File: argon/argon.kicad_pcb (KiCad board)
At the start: 2 copper layers, 60 x 60 mm, 77 parts, among them J1 USB, J2 V3V3-GND, J3 V3V3-GND, J4 V3V3-GND, J5 V3V3-GND, J6 V3V3-GND, J7 V3V3-GND, U1 LMC555xM, U2 AMS1117-3.3, U3 93LCxxA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

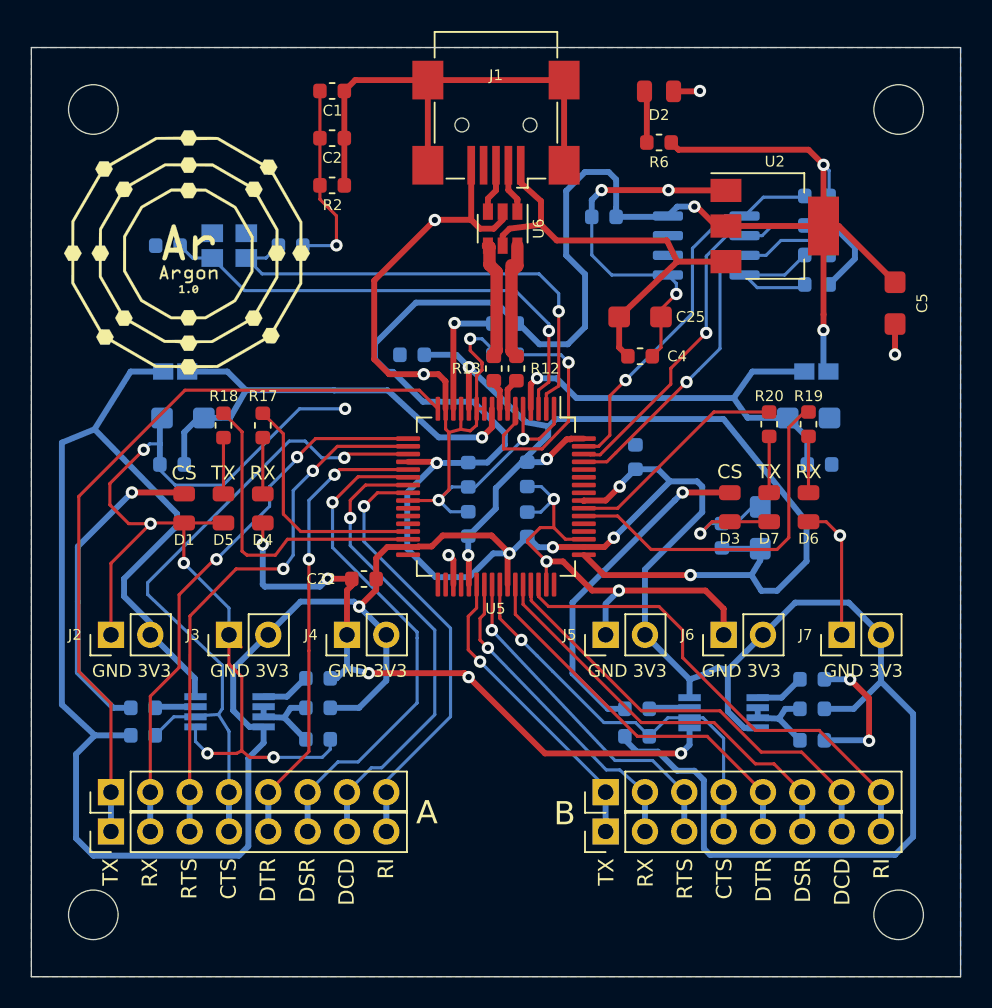
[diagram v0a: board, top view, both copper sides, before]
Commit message: GND on front & fix paths
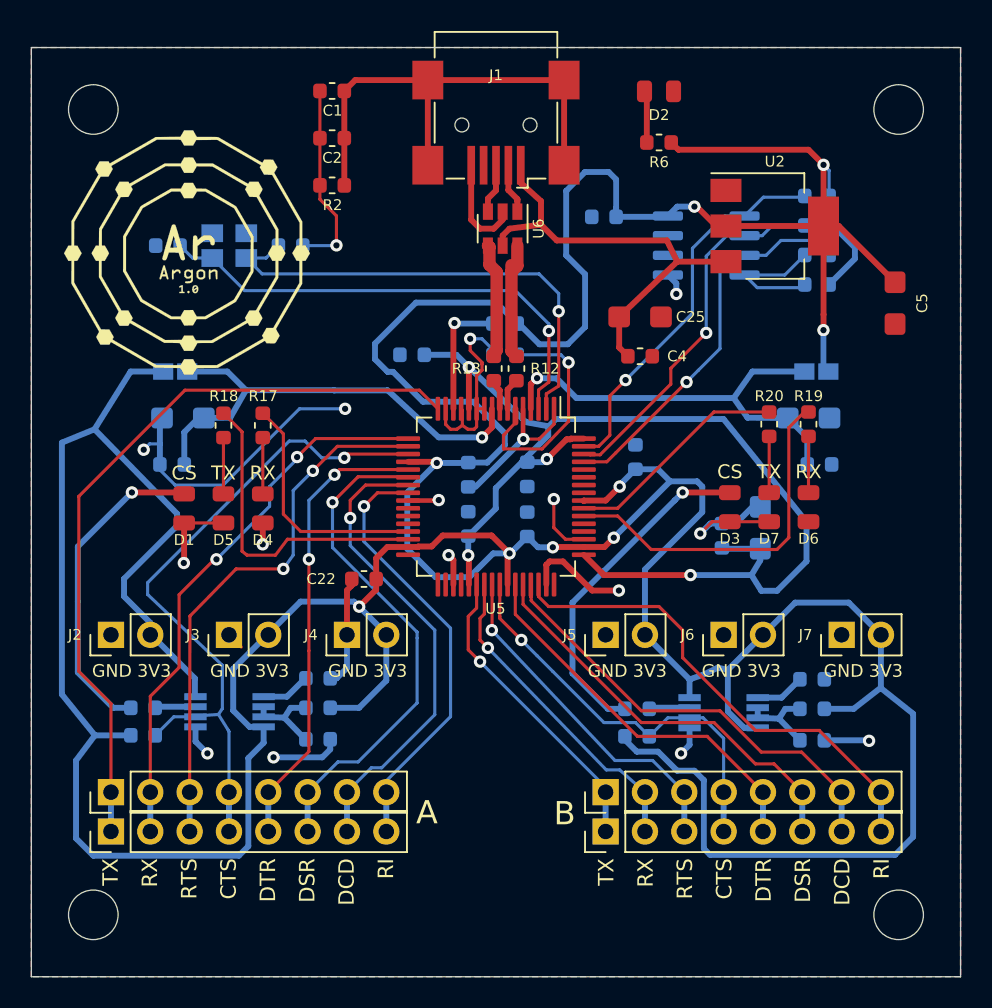
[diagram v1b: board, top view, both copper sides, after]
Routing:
- net GND: track 273.3 -> 114.4 mm, vias 30 -> 17
- net V3V3: track 343.0 -> 342.4 mm
- added copper zone on F.Cu, net GND

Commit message: Move capacitor & add filled zone near USB
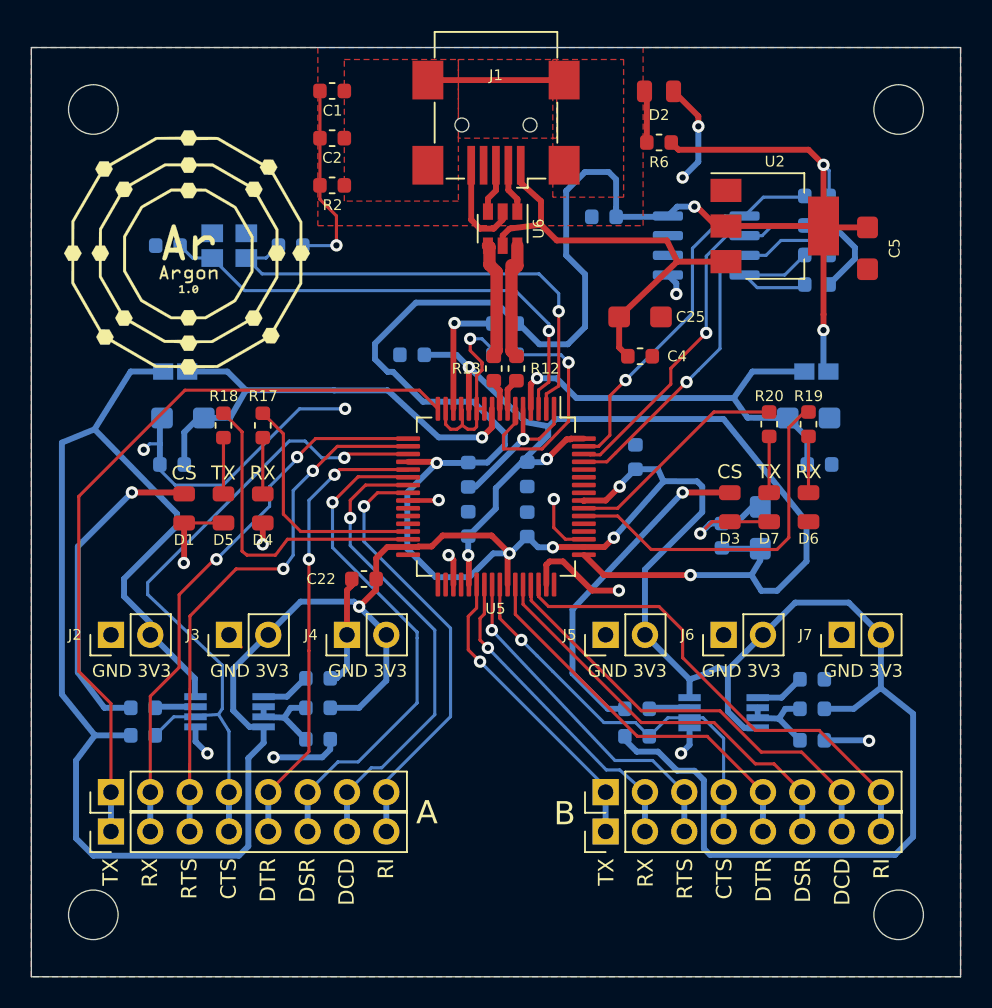
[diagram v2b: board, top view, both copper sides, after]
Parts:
- moved C5 3.96 mm to (174.0, 93.0)
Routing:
- net Net-(C1-Pad2): track 31.6 -> 8.80 mm
- net GND: track 114.4 -> 121.0 mm, vias 17 -> 19
- net V3V3: track 342.4 -> 339.1 mm
- added copper zone on F.Cu, net Net-(C1-Pad2)

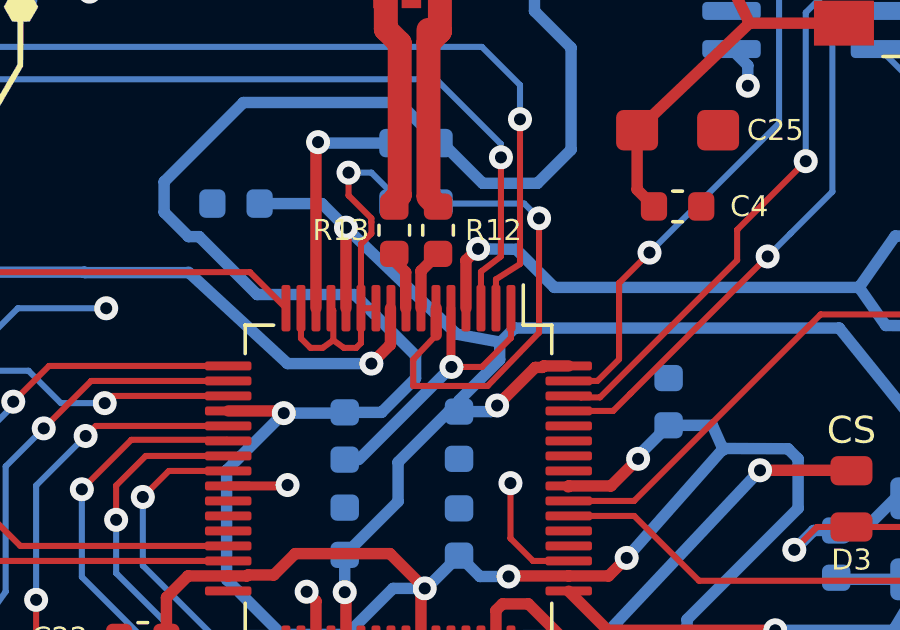
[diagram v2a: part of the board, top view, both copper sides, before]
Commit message: Fix connected pins on ftdi
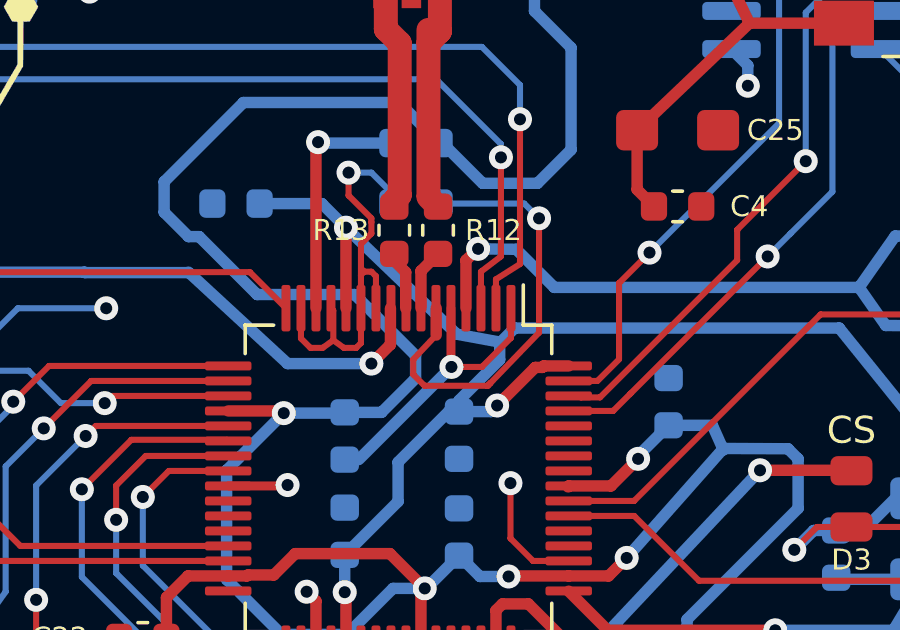
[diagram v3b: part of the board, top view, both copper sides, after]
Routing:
- net GND: track 121.0 -> 122.4 mm
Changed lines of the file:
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@@
     (thickness 1.6)
     (drawings 46)
-    (tracks 703)
+    (tracks 713)
     (zones 0)
     (modules 77)
@@
     (0 F.Cu signal)
     (31 B.Cu signal)
-    (32 B.Adhes user)
-    (33 F.Adhes user)
+    (32 B.Adhes user hide)
+    (33 F.Adhes user hide)
     (34 B.Paste user)
     (35 F.Paste user hide)
-    (36 B.SilkS user)
+    (36 B.SilkS user hide)
     (37 F.SilkS user)
-    (38 B.Mask user)
+    (38 B.Mask user hide)
     (39 F.Mask user hide)
     (40 Dwgs.User user)
-    (41 Cmts.User user)
+    (41 Cmts.User user hide)
     (42 Eco1.User user hide)
-    (43 Eco2.User user)
+    (43 Eco2.User user hide)
     (44 Edge.Cuts user)
     (45 Margin user hide)
@@
   )
   (setup
-    (last_trace_width 0.381)
+    (last_trace_width 0.2032)
     (user_trace_width 0.2032)
     (user_trace_width 0.3)
@@
   (segment (start 139.3 120.7295) (end 139.7105 120.7295) (width 0.381) (layer B.Cu) (net 1))
   (segment (start 130.5975 123.8635) (end 130.9755 123.8635) (width 0.381) (layer B.Cu) (net 1))
-  (segment (start 148.75 103.325) (end 148.75 101.186) (width 0.2032) (layer F.Cu) (net 1))
   (segment (start 148.75 101.186) (end 149.098 100.838) (width 0.2032) (layer F.Cu) (net 1))
   (segment (start 149.098 100.838) (end 149.098 100.457) (width 0.2032) (layer F.Cu) (net 1))
@@
   (segment (start 149.098 100.33) (end 148.336 99.568) (width 0.2032) (layer F.Cu) (net 1))
   (segment (start 148.336 99.568) (end 148.336 98.806) (width 0.2032) (layer F.Cu) (net 1))
-  (segment (start 149.25 103.325) (end 148.75 103.325) (width 0.2032) (layer F.Cu) (net 1))
   (segment (start 167.64 110.6175) (end 165.1 110.6175) (width 0.2032) (layer F.Cu) (net 1))
   (segment (start 165.1 110.6175) (end 163.9565 110.6175) (width 0.2032) (layer F.Cu) (net 1))
@@
   (via (at 162.052 88.392) (size 0.8) (drill 0.4) (layers F.Cu B.Cu) (net 1))
   (segment (start 163.068 87.376) (end 162.052 88.392) (width 0.381) (layer B.Cu) (net 1))
+  (segment (start 149.25 103.325) (end 149.25 102.26) (width 0.2032) (layer F.Cu) (net 1))
+  (segment (start 149.25 102.26) (end 149.098 102.108) (width 0.2032) (layer F.Cu) (net 1))
+  (segment (start 148.858 102.108) (end 148.75 102) (width 0.2032) (layer F.Cu) (net 1))
+  (segment (start 149.098 102.108) (end 148.858 102.108) (width 0.2032) (layer F.Cu) (net 1))
+  (segment (start 148.75 102) (end 148.75 101.186) (width 0.2032) (layer F.Cu) (net 1))
+  (segment (start 148.75 102.216) (end 148.858 102.108) (width 0.2032) (layer F.Cu) (net 1))
+  (segment (start 148.75 102.25) (end 148.75 102) (width 0.2032) (layer F.Cu) (net 1))
+  (segment (start 148.75 102.25) (end 148.75 102.216) (width 0.2032) (layer F.Cu) (net 1))
+  (segment (start 148.75 103.325) (end 148.75 102.25) (width 0.2032) (layer F.Cu) (net 1))
   (segment (start 136.503 121.9135) (end 137.687 120.7295) (width 0.381) (layer B.Cu) (net 2))
   (segment (start 134.9595 121.9135) (end 136.503 121.9135) (width 0.381) (layer B.Cu) (net 2))
@@
   (segment (start 154.686 100.33) (end 154.194 99.838) (width 0.2032) (layer B.Cu) (net 9))
   (segment (start 154.686 104.14) (end 154.686 100.33) (width 0.2032) (layer F.Cu) (net 9))
-  (segment (start 152.9715 105.918) (end 154.686 104.14) (width 0.2032) (layer F.Cu) (net 9))
-  (segment (start 150.495 105.918) (end 152.9715 105.918) (width 0.2032) (layer F.Cu) (net 9))
   (segment (start 151.25801 104.22051) (end 150.495 105.029) (width 0.2032) (layer F.Cu) (net 9))
-  (segment (start 150.495 105.029) (end 150.495 105.918) (width 0.2032) (layer F.Cu) (net 9))
+  (segment (start 150.495 105.029) (end 150.495 105.537) (width 0.2032) (layer F.Cu) (net 9))
+  (segment (start 152.974437 105.911601) (end 153.065019 105.821019) (width 0.2032) (layer F.Cu) (net 9))
+  (segment (start 150.869601 105.911601) (end 152.974437 105.911601) (width 0.2032) (layer F.Cu) (net 9))
+  (segment (start 150.495 105.537) (end 150.869601 105.911601) (width 0.2032) (layer F.Cu) (net 9))
+  (segment (start 152.9715 105.918) (end 153.065019 105.821019) (width 0.2032) (layer F.Cu) (net 9))
+  (segment (start 153.065019 105.821019) (end 154.686 104.14) (width 0.2032) (layer F.Cu) (net 9))
   (via (at 141.478 109.617) (size 0.8) (drill 0.4) (layers F.Cu B.Cu) (net 10))
   (segment (start 142.345 108.75) (end 144.325 108.75) (width 0.2032) (layer F.Cu) (net 10))

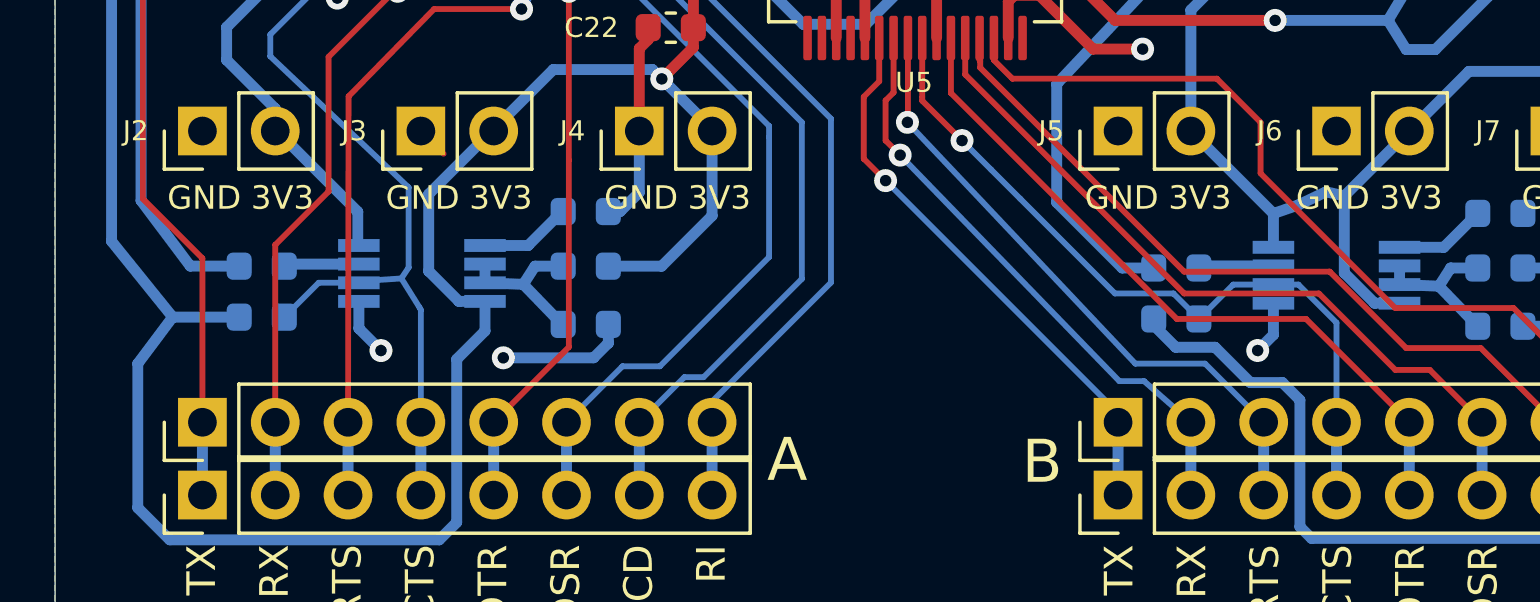
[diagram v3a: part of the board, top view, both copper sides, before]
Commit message: Add labels
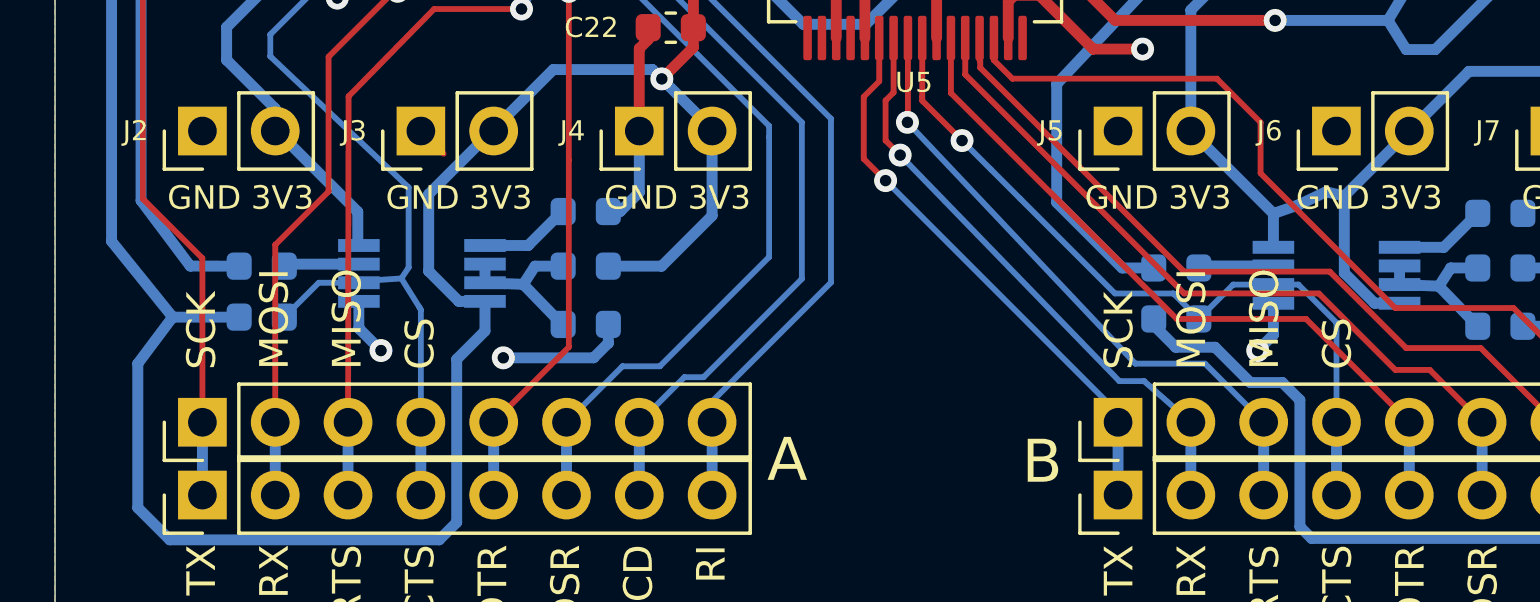
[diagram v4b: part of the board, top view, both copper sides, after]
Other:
- board text added: "MISO"
- board text added: "MOSI"
- board text added: "SCK"
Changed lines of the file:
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@@
   (general
     (thickness 1.6)
-    (drawings 46)
+    (drawings 54)
     (tracks 713)
     (zones 0)
@@
   (layers
     (0 F.Cu signal)
-    (31 B.Cu signal)
+    (31 B.Cu signal hide)
     (32 B.Adhes user hide)
     (33 F.Adhes user hide)
-    (34 B.Paste user)
+    (34 B.Paste user hide)
     (35 F.Paste user hide)
     (36 B.SilkS user hide)
@@
     (pad 8 thru_hole oval (at 0 17.78 90) (size 1.7 1.7) (drill 1) (layers *.Cu *.Mask)
       (net 45 "Net-(S2-Pad8)"))
-    (model ${KISYS3DMOD}/Connector_PinHeader_2.54mm.3dshapes/PinHeader_1x04_P2.54mm_Vertical.wrl
-      (offset (xyz 0 -10.2 0))
-      (scale (xyz 1 1 1))
-      (rotate (xyz 0 0 0))
-    )
-    (model ${KISYS3DMOD}/Connector_PinSocket_2.54mm.3dshapes/PinSocket_1x04_P2.54mm_Vertical.wrl
+    (model ${KISYS3DMOD}/Connector_PinSocket_2.54mm.3dshapes/PinSocket_1x08_P2.54mm_Vertical.wrl
       (at (xyz 0 0 0))
       (scale (xyz 1 1 1))
@@
     )
   )
+  (gr_text MOSI (at 159.654 126.25 90) (layer F.SilkS)
+    (effects (font (size 1 1) (thickness 0.2)) (justify left))
+  )
+  (gr_text MISO (at 162.194 126.25 90) (layer F.SilkS)
+    (effects (font (size 1 1) (thickness 0.2)) (justify left))
+  )
+  (gr_text SCK (at 157.114 126.25 90) (layer F.SilkS)
+    (effects (font (size 1 1) (thickness 0.2)) (justify left))
+  )
+  (gr_text CS (at 164.734 126.25 90) (layer F.SilkS)
+    (effects (font (size 1 1) (thickness 0.2)) (justify left))
+  )
+  (gr_text CS (at 132.734 126.25 90) (layer F.SilkS)
+    (effects (font (size 1 1) (thickness 0.2)) (justify left))
+  )
+  (gr_text MISO (at 130.194 126.25 90) (layer F.SilkS)
+    (effects (font (size 1 1) (thickness 0.2)) (justify left))
+  )
+  (gr_text MOSI (at 127.654 126.25 90) (layer F.SilkS)
+    (effects (font (size 1 1) (thickness 0.2)) (justify left))
+  )
+  (gr_text SCK (at 125.114 126.25 90) (layer F.SilkS)
+    (effects (font (size 1 1) (thickness 0.2)) (justify left))
+  )
   (dimension 60 (width 0.15) (layer Dwgs.User)
